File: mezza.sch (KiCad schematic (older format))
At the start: 2 parts, among them P1 CONN_02X20, P2 CONN_02X20

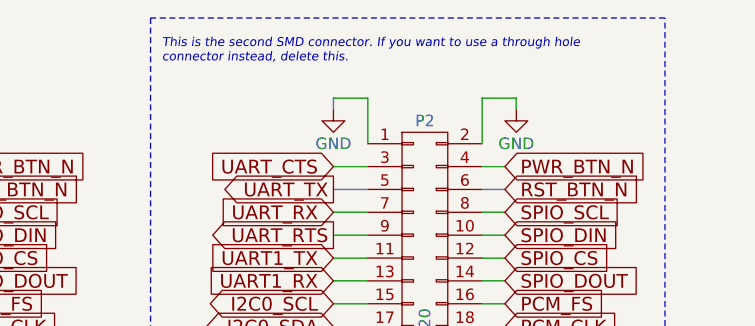
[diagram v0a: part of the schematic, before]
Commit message: Refine Schematic Notes and Update Cache
Comment on changing the footprint for using a through hole connector (rather
than the surface mount) has been refined and made easier to understand.
Cached library version has been updated.

Signed-off-by: Sophie Haynes <sophie.haynes@linaro.org>
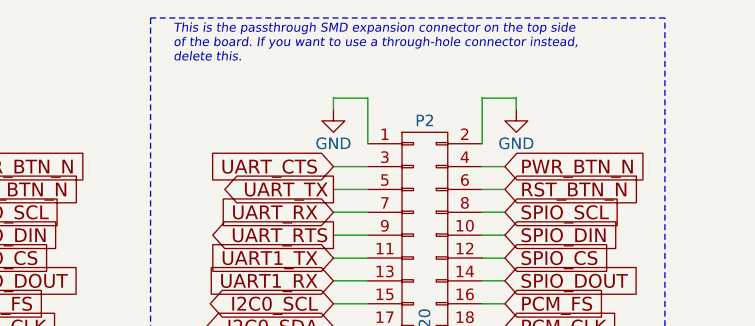
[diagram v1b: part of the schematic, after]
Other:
- note added: "This is the passthrough SMD expansion connector on the top side\nof the board. If you want to use a through-hole connector instead,\ndelete this."
- note removed: "This is the second SMD connector. If you want to use a through hole \nconnector instead, delete this.\n"
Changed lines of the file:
@@
 LIBS:contrib
 LIBS:valves
+LIBS:mezza-cache
 EELAYER 25 0
 EELAYER END
@@
 Wire Wire Line
 	1650 1500 1500 1500
-Text Notes 3200 750  0    39   Italic 0
-This is the second SMD connector. If you want to use a through hole \nconnector instead, delete this.\n
+Text Notes 3250 750  0    39   Italic 0
+This is the passthrough SMD expansion connector on the top side\nof the board. If you want to use a through-hole connector instead,\ndelete this.
 Wire Notes Line
 	5400 3200 5400 550

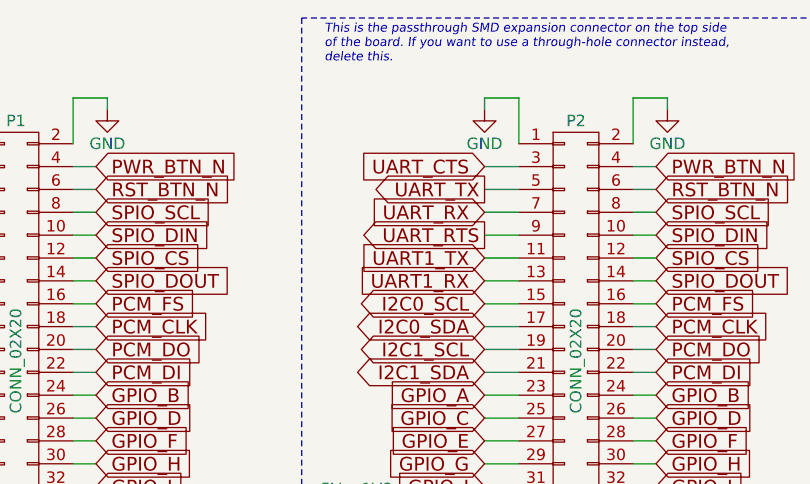
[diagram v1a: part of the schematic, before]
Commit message: Update P1/2 Footprints
The footprints used were outdated and therefore have now been updated to the
correct ones.
In the schematic, the connectors were incorrectly assigned
footprints. This has been rectified.
The 96boards.lib file has been cleaned up so that it only contains the
required connector for this project.

Signed-off-by: Sophie Haynes <sophie.haynes@linaro.org>
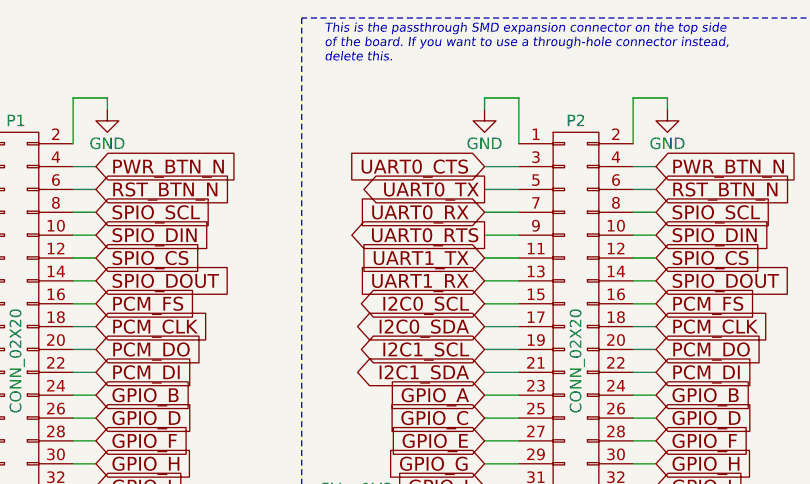
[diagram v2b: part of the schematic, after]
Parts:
- P1: footprint 96boards:Socket_Strip_SMD_2x20_Pitch2mm -> 96boards:Pin_Header_Straight_2x20_Pitch2mm
- P2: footprint 96boards:Pin_Header_SMD_2x20_Pitch2mm -> 96boards:Socket_Strip_Straight_2x20_Pitch2mm
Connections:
- net UART_CTS is gone; now on net UART0_CTS: P2.3 (P3)
- net UART_RTS is gone; now on net UART0_RTS: P2.9 (P9)
- net UART_RX is gone; now on net UART0_RX: P2.7 (P7)
- net UART_TX is gone; now on net UART0_TX: P2.5 (P5)
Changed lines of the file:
@@
 EESchema Schematic File Version 2
+LIBS:96boards-cache
 LIBS:power
 LIBS:device
@@
 LIBS:contrib
 LIBS:valves
+LIBS:96boards
 LIBS:mezza-cache
 EELAYER 25 0
@@
 F 0 "P1" H 1900 3100 50  0000 C CNN
 F 1 "CONN_02X20" V 1900 2050 50  0000 C CNN
-F 2 "96boards:Socket_Strip_SMD_2x20_Pitch2mm" H 1900 1100 60  0001 C CNN
+F 2 "96boards:Pin_Header_Straight_2x20_Pitch2mm" H 1900 1100 60  0001 C CNN
 F 3 "" H 1900 1100 60  0000 C CNN
 F 4 "Yxcon" H 1900 2050 60  0001 C CNN "Mfr"
@@
 $EndComp
 Text GLabel 3950 1500 0    60   Output ~ 0
-UART_RTS
+UART0_RTS
 Text GLabel 1500 2100 0    60   BiDi ~ 0
 I2C1_SDA
@@
 $EndComp
 Text GLabel 3950 1300 0    60   Output ~ 0
-UART_TX
+UART0_TX
 $Comp
 L GND #PWR08
@@
 $EndComp
 Text GLabel 3950 1200 0    60   Input ~ 0
-UART_CTS
+UART0_CTS
 Text GLabel 2250 1200 2    60   Input ~ 0
 PWR_BTN_N
@@
 F 0 "P2" H 4350 3100 50  0000 C CNN
 F 1 "CONN_02X20" V 4350 2050 50  0000 C CNN
-F 2 "96boards:Pin_Header_SMD_2x20_Pitch2mm" H 4350 1100 60  0001 C CNN
+F 2 "96boards:Socket_Strip_Straight_2x20_Pitch2mm" H 4350 1100 60  0001 C CNN
 F 3 "" H 4350 1100 60  0000 C CNN
 F 4 "Yxcon" H 4350 2050 60  0001 C CNN "Mfr"
@@
 GPIO_B
 Text GLabel 3950 1400 0    60   Input ~ 0
-UART_RX
+UART0_RX
 Text Notes 2650 3400 0    60   ~ 0
 Expansion Connectors

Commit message: Default to SMD footprints on layout
Default to using SMD connectors on the layout. The user can choose to
switch to through-hole connectors if they so desire by deleting one of
the schematic objects and switching the footprint.

Signed-off-by: Grant Likely <grant.likely@linaro.org>
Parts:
- P1: footprint 96boards:Pin_Header_Straight_2x20_Pitch2mm -> 96boards:Pin_Header_SMD_2x20_Pitch2mm
- P2: footprint 96boards:Socket_Strip_Straight_2x20_Pitch2mm -> 96boards:Socket_Strip_SMD_2x20_Pitch2mm
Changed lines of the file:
@@
 EESchema Schematic File Version 2
-LIBS:96boards-cache
 LIBS:power
 LIBS:device
@@
 F 0 "P2" H 4350 3100 50  0000 C CNN
 F 1 "CONN_02X20" V 4350 2050 50  0000 C CNN
-F 2 "96boards:Socket_Strip_Straight_2x20_Pitch2mm" H 4350 1100 60  0001 C CNN
+F 2 "96boards:Socket_Strip_SMD_2x20_Pitch2mm" H 4350 1100 60  0001 C CNN
 F 3 "" H 4350 1100 60  0000 C CNN
 F 4 "Yxcon" H 4350 2050 60  0001 C CNN "Mfr"
@@
 	700  3250 2950 3250
 $Comp
-L GND #PWR01
+L GND #PWR07
 U 1 1 55BEAA68
 P 1500 950
-F 0 "#PWR01" H 1500 700 50  0001 C CNN
+F 0 "#PWR07" H 1500 700 50  0001 C CNN
 F 1 "GND" H 1500 800 50  0000 C CNN
 F 2 "" H 1500 950 60  0000 C CNN
@@
 $EndComp
 $Comp
-L GND #PWR02
+L GND #PWR08
 U 1 1 55BEA10A
 P 1550 3000
-F 0 "#PWR02" H 1550 2750 50  0001 C CNN
+F 0 "#PWR08" H 1550 2750 50  0001 C CNN
 F 1 "GND" H 1550 2850 50  0000 C CNN
 F 2 "" H 1550 3000 60  0000 C CNN
@@
 $EndComp
 $Comp
-L GND #PWR03
+L GND #PWR09
 U 1 1 55BEA0BC
 P 2250 3000
-F 0 "#PWR03" H 2250 2750 50  0001 C CNN
+F 0 "#PWR09" H 2250 2750 50  0001 C CNN
 F 1 "GND" H 2250 2850 50  0000 C CNN
 F 2 "" H 2250 3000 60  0000 C CNN
@@
 SYS_DCIN
 $Comp
-L GND #PWR04
+L GND #PWR010
 U 1 1 55D43BD4
 P 2300 950
-F 0 "#PWR04" H 2300 700 50  0001 C CNN
+F 0 "#PWR010" H 2300 700 50  0001 C CNN
 F 1 "GND" H 2300 800 50  0000 C CNN
 F 2 "" H 2300 950 60  0000 C CNN
@@
 F 0 "P1" H 1900 3100 50  0000 C CNN
 F 1 "CONN_02X20" V 1900 2050 50  0000 C CNN
-F 2 "96boards:Pin_Header_Straight_2x20_Pitch2mm" H 1900 1100 60  0001 C CNN
+F 2 "96boards:Pin_Header_SMD_2x20_Pitch2mm" H 1900 1100 60  0001 C CNN
 F 3 "" H 1900 1100 60  0000 C CNN
 F 4 "Yxcon" H 1900 2050 60  0001 C CNN "Mfr"
@@
 $EndComp
 $Comp
-L +1V8 #PWR05
+L +1V8 #PWR011
 U 1 1 55D43CFB
 P 1000 2750
-F 0 "#PWR05" H 1000 2600 50  0001 C CNN
+F 0 "#PWR011" H 1000 2600 50  0001 C CNN
 F 1 "+1V8" H 1000 2890 50  0000 C CNN
 F 2 "" H 1000 2750 60  0000 C CNN
@@
 $EndComp
 $Comp
-L +5V #PWR06
+L +5V #PWR012
 U 1 1 55D440FD
 P 800 2750
-F 0 "#PWR06" H 800 2600 50  0001 C CNN
+F 0 "#PWR012" H 800 2600 50  0001 C CNN
 F 1 "+5V" H 800 2890 50  0000 C CNN
 F 2 "" H 800 2750 60  0000 C CNN

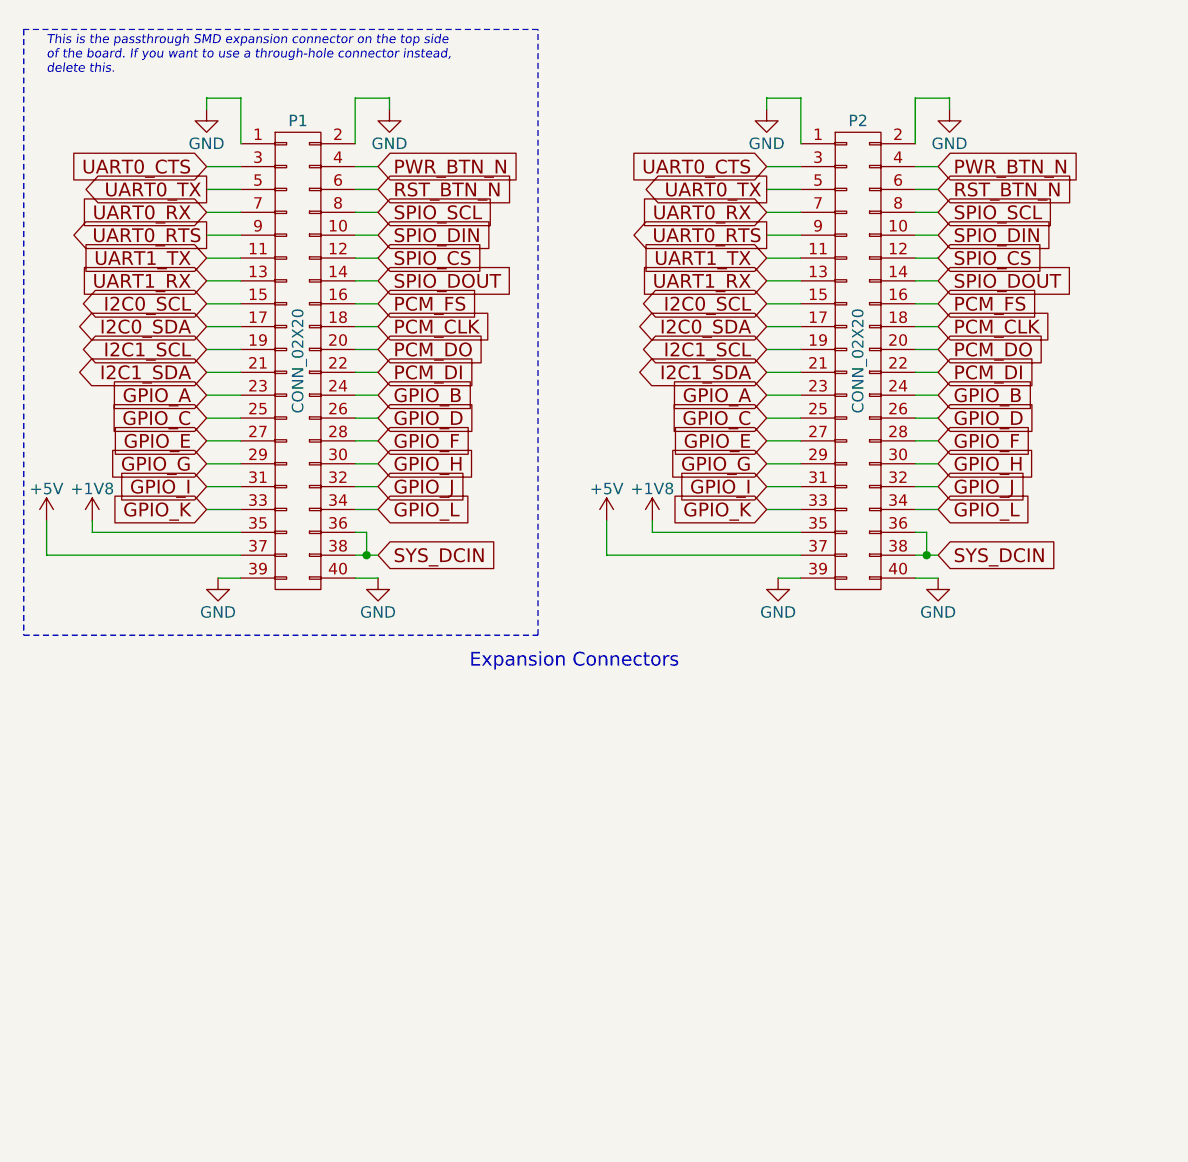
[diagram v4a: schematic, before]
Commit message: Improve documentation on SMD vs. through-hole connectors
Add a note to the schematic that describes how to select between SMD and
through-hole 2x20 Low-speed expansion connector.

Signed-off-by: Grant Likely <grant.likely@linaro.org>
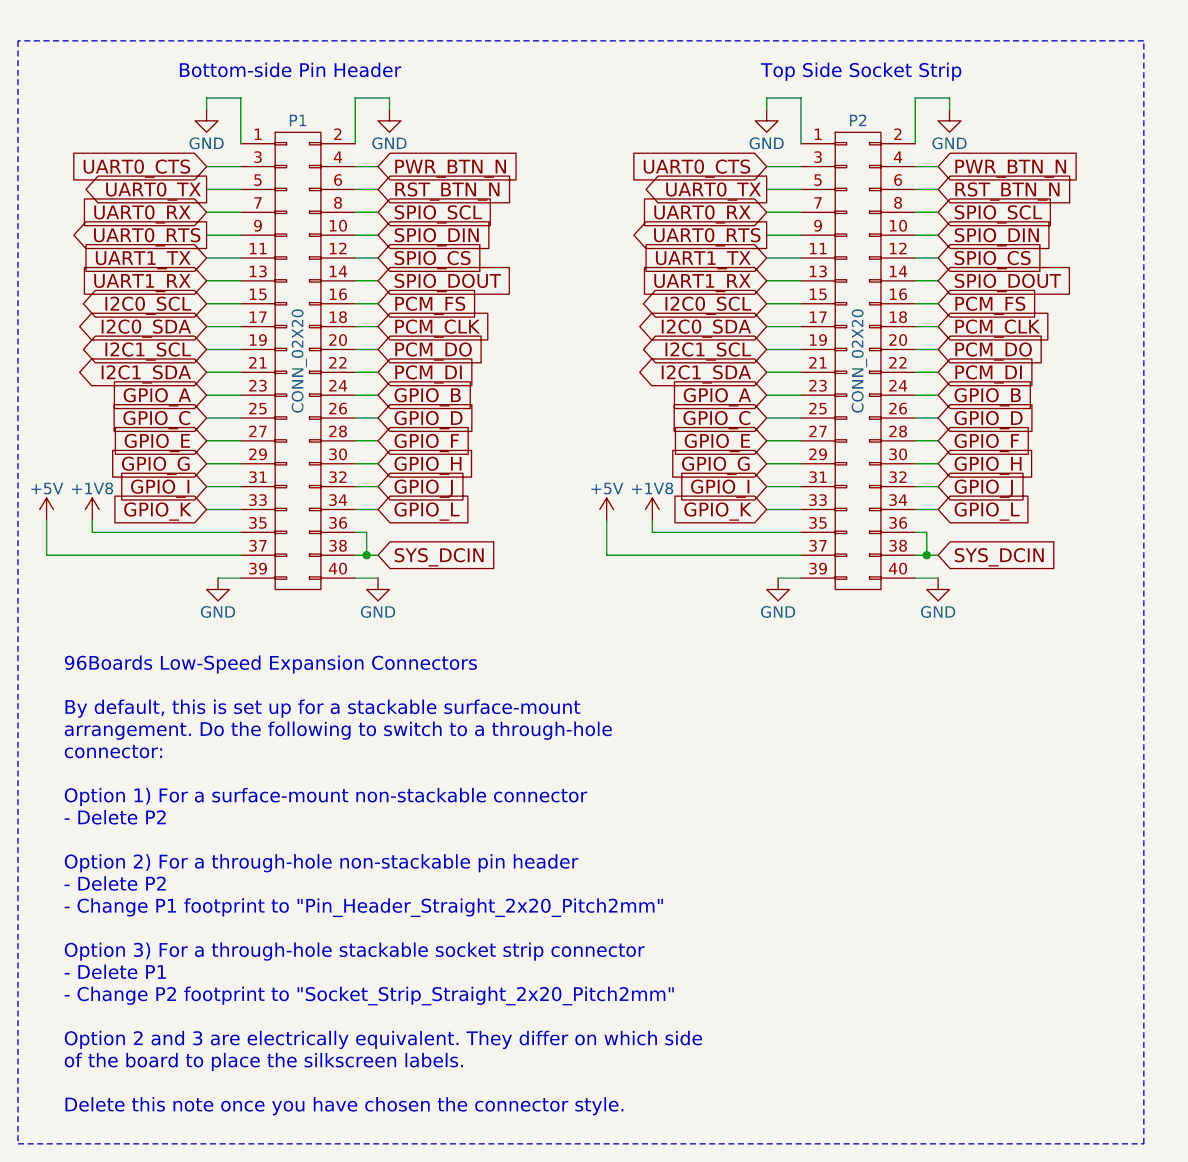
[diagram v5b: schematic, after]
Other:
- note added: "96Boards Low-Speed Expansion Connectors\n\nBy default, this is set up for a stackable surface-mount\narrangement. Do the following to switch to a through-hole\nconnector:\n\nOption 1) For a surface-mount non-stackable connector\n- Delete P2\n\nOption 2) For a through-hole non-stackable pin header\n- Delete P2\n- Change P1 footprint to "Pin_Header_Straight_2x20_Pitch2mm"\n\nOption 3) For a through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"
- note added: "Bottom-side Pin Header"
- note added: "Top Side Socket Strip"
- note removed: "Expansion Connectors"
- note removed: "This is the passthrough SMD expansion connector on the top side\nof the board. If you want to use a through-hole connector instead,\ndelete this."
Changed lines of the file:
@@
 Text GLabel 3950 1400 0    60   Input ~ 0
 UART0_RX
-Text Notes 2650 3400 0    60   ~ 0
-Expansion Connectors
+Text Notes 875  5350 0    60   ~ 0
+96Boards Low-Speed Expansion Connectors\n\nBy default, this is set up for a stackable surface-mount\narrangement. Do the following to switch to a through-hole\nconnector:\n\nOption 1) For a surface-mount non-stackable connector\n- Delete P2\n\nOption 2) For a through-hole non-stackable pin header\n- Delete P2\n- Change P1 footprint to "Pin_Header_Straight_2x20_Pitch2mm"\n\nOption 3) For a through-hole stackable socket strip connector\n- Delete P1\n- Change P2 footprint to "Socket_Strip_Straight_2x20_Pitch2mm"\n\nOption 2 and 3 are electrically equivalent. They differ on which side\nof the board to place the silkscreen labels.\n\nDelete this note once you have chosen the connector style.
 Text GLabel 4700 1200 2    60   Input ~ 0
 PWR_BTN_N
@@
 Wire Wire Line
 	4100 1500 3950 1500
-Text Notes 800  800  0    39   Italic 0
-This is the passthrough SMD expansion connector on the top side\nof the board. If you want to use a through-hole connector instead,\ndelete this.
-Wire Notes Line
-	2950 3250 2950 600
-Wire Notes Line
-	2950 600  700  600
-Wire Notes Line
-	700  600  700  3250
-Wire Notes Line
-	700  3250 2950 3250
 $Comp
 L GND #PWR07
@@
 Wire Wire Line
 	1650 1500 1500 1500
+Text Notes 1375 825  0    60   ~ 0
+Bottom-side Pin Header
+Text Notes 3925 825  0    60   ~ 0
+Top Side Socket Strip
+Wire Notes Line
+	675  650  675  5475
+Wire Notes Line
+	675  5475 5600 5475
+Wire Notes Line
+	5600 5475 5600 650
+Wire Notes Line
+	5600 650  675  650
 $EndSCHEMATC
